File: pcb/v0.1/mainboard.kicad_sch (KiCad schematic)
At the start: 9 parts, among them J11 USB_C_Receptacle_fw, J12 Conn_01x02_Pin, J6 Conn_01x04_Pin, U6 AP2112K-3.3TRG1

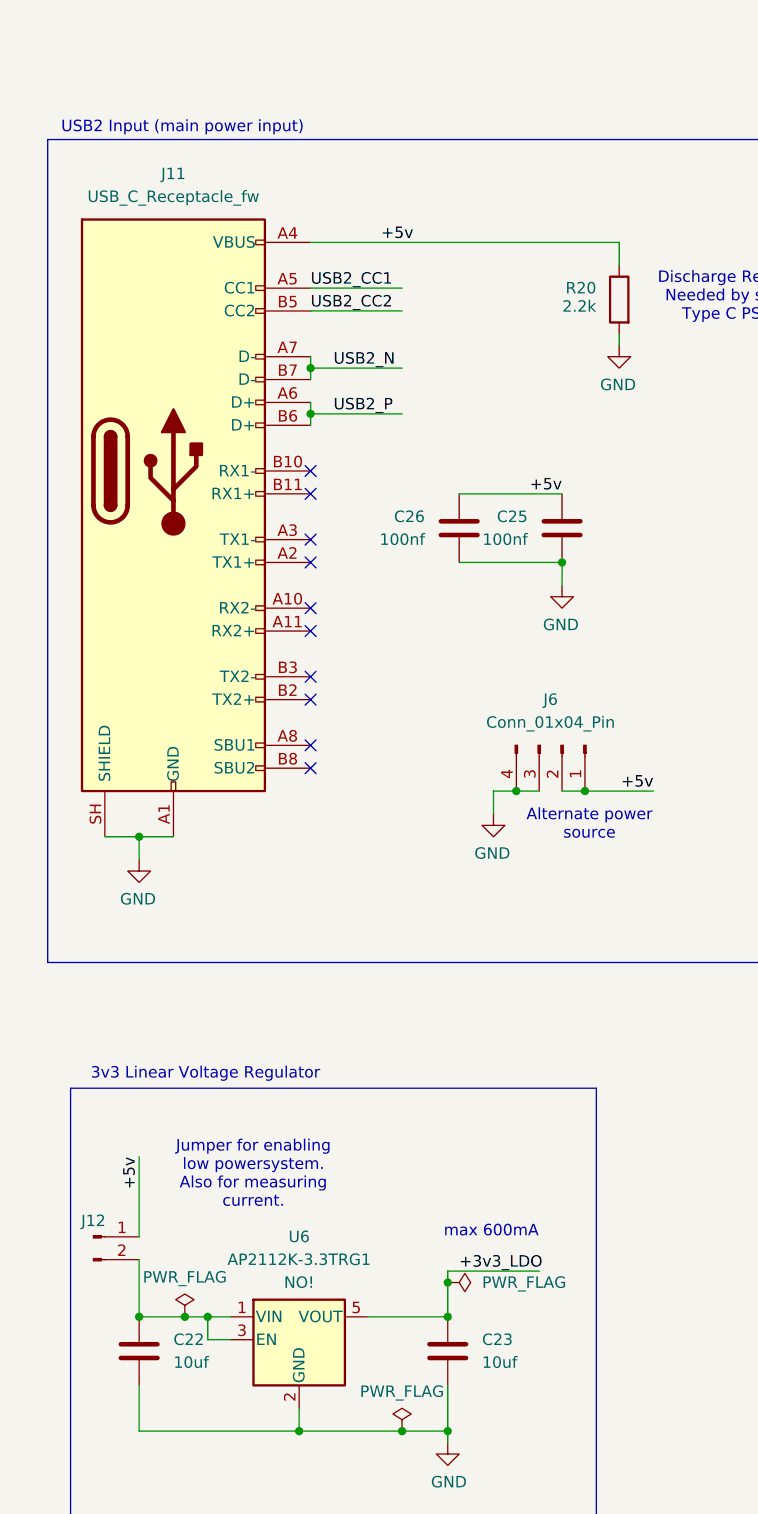
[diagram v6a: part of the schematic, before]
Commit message: Add pullup for nRESET of the nRF.
Also re-annotated all of the symbol numbers as they were starting to get
out of hand.
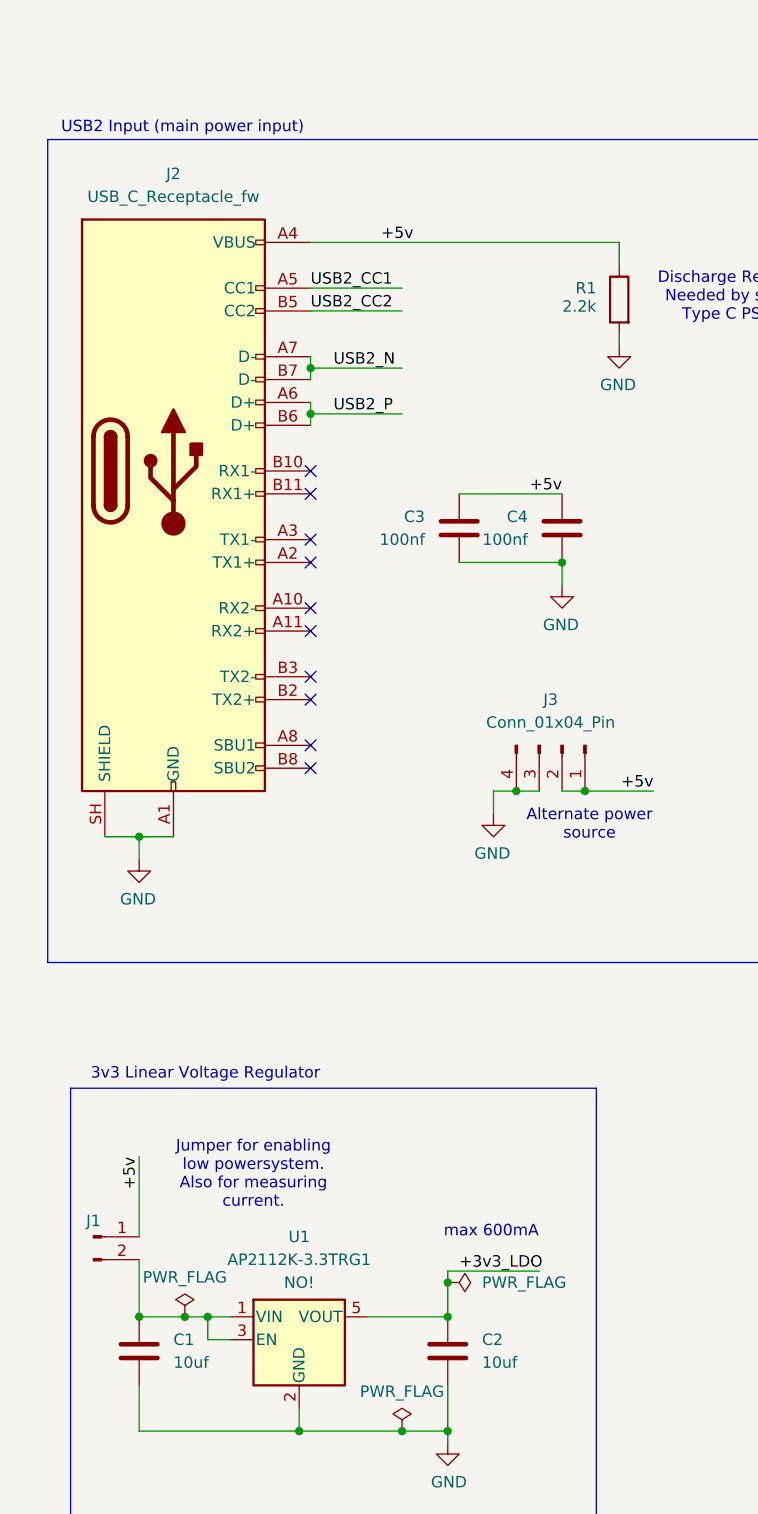
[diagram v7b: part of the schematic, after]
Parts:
- renumbered C22 to C1, C23 to C2, C26 to C3, C25 to C4, J12 to J1, J11 to J2, J6 to J3, R20 to R1, U6 to U1
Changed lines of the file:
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@@
 		(dnp no)
 		(fields_autoplaced yes)
-		(property "Reference" "C26"
+		(property "Reference" "C3"
 			(at 62.23 71.12 0)
 			(show_name no)
@@
 			(project "mainboard"
 				(path "/5b8aa782-5c3d-43e7-a869-3bd000015f52"
-					(reference "C26")
+					(reference "C3")
 					(unit 1)
 				)
@@
 		(dnp no)
 		(fields_autoplaced yes)
-		(property "Reference" "C22"
+		(property "Reference" "C1"
 			(at 34.29 162.5599 0)
 			(show_name no)
@@
 			(project "mainboard"
 				(path "/5b8aa782-5c3d-43e7-a869-3bd000015f52"
-					(reference "C22")
+					(reference "C1")
 					(unit 1)
 				)
@@
 		(in_pos_files yes)
 		(dnp no)
-		(property "Reference" "J12"
+		(property "Reference" "J1"
 			(at 25.4 149.352 0)
 			(show_name no)
@@
 			(project "mainboard"
 				(path "/5b8aa782-5c3d-43e7-a869-3bd000015f52"
-					(reference "J12")
+					(reference "J1")
 					(unit 1)
 				)
@@
 		(in_pos_files yes)
 		(dnp no)
-		(property "Reference" "#PWR040"
+		(property "Reference" "#PWR02"
 			(at 64.77 180.34 0)
 			(hide yes)
@@
 			(project "mainboard"
 				(path "/5b8aa782-5c3d-43e7-a869-3bd000015f52"
-					(reference "#PWR040")
+					(reference "#PWR02")
 					(unit 1)
 				)
@@
 		(in_pos_files yes)
 		(dnp no)
-		(property "Reference" "#PWR047"
+		(property "Reference" "#PWR01"
 			(at 30.48 115.57 0)
 			(hide yes)
@@
 			(project "mainboard"
 				(path "/5b8aa782-5c3d-43e7-a869-3bd000015f52"
-					(reference "#PWR047")
+					(reference "#PWR01")
 					(unit 1)
 				)
@@
 		(in_pos_files yes)
 		(dnp no)
-		(property "Reference" "R20"
+		(property "Reference" "R1"
 			(at 81.28 45.72 0)
 			(show_name no)
@@
 			(project "mainboard"
 				(path "/5b8aa782-5c3d-43e7-a869-3bd000015f52"
-					(reference "R20")
+					(reference "R1")
 					(unit 1)
 				)
@@
 		(in_pos_files yes)
 		(dnp no)
-		(property "Reference" "#PWR048"
+		(property "Reference" "#PWR03"
 			(at 69.85 110.49 0)
 			(hide yes)
@@
 			(project "mainboard"
 				(path "/5b8aa782-5c3d-43e7-a869-3bd000015f52"
-					(reference "#PWR048")
+					(reference "#PWR03")
 					(unit 1)
 				)
@@
 		(dnp no)
 		(fields_autoplaced yes)
-		(property "Reference" "C23"
+		(property "Reference" "C2"
 			(at 68.58 162.5599 0)
 			(show_name no)
@@
 			(project "mainboard"
 				(path "/5b8aa782-5c3d-43e7-a869-3bd000015f52"
-					(reference "C23")
+					(reference "C2")
 					(unit 1)
 				)
@@
 		(dnp no)
 		(fields_autoplaced yes)
-		(property "Reference" "U6"
+		(property "Reference" "U1"
 			(at 48.26 151.13 0)
 			(show_name no)
@@
 			(project "mainboard"
 				(path "/5b8aa782-5c3d-43e7-a869-3bd000015f52"
-					(reference "U6")
+					(reference "U1")
 					(unit 1)
 				)
@@
 		(dnp no)
 		(fields_autoplaced yes)
-		(property "Reference" "J6"
+		(property "Reference" "J3"
 			(at 76.2 91.44 90)
 			(show_name no)
@@
 			(project "mainboard"
 				(path "/5b8aa782-5c3d-43e7-a869-3bd000015f52"
-					(reference "J6")
+					(reference "J3")
 					(unit 1)
 				)
@@
 		(dnp no)
 		(fields_autoplaced yes)
-		(property "Reference" "C25"
+		(property "Reference" "C4"
 			(at 73.66 71.12 0)
 			(show_name no)
@@
 			(project "mainboard"
 				(path "/5b8aa782-5c3d-43e7-a869-3bd000015f52"
-					(reference "C25")
+					(reference "C4")
 					(unit 1)
 				)
@@
 		(in_pos_files yes)
 		(dnp no)
-		(property "Reference" "#PWR039"
+		(property "Reference" "#PWR04"
 			(at 77.47 85.09 0)
 			(hide yes)
@@
 			(project "mainboard"
 				(path "/5b8aa782-5c3d-43e7-a869-3bd000015f52"
-					(reference "#PWR039")
+					(reference "#PWR04")
 					(unit 1)
 				)
@@
 		(in_pos_files yes)
 		(dnp no)
-		(property "Reference" "J11"
+		(property "Reference" "J2"
 			(at 34.29 33.02 0)
 			(show_name no)
@@
 			(project "mainboard"
 				(path "/5b8aa782-5c3d-43e7-a869-3bd000015f52"
-					(reference "J11")
+					(reference "J2")
 					(unit 1)
 				)
@@
 		(in_pos_files yes)
 		(dnp no)
-		(property "Reference" "#PWR046"
+		(property "Reference" "#PWR05"
 			(at 83.82 58.42 0)
 			(hide yes)
@@
 			(project "mainboard"
 				(path "/5b8aa782-5c3d-43e7-a869-3bd000015f52"
-					(reference "#PWR046")
+					(reference "#PWR05")
 					(unit 1)
 				)

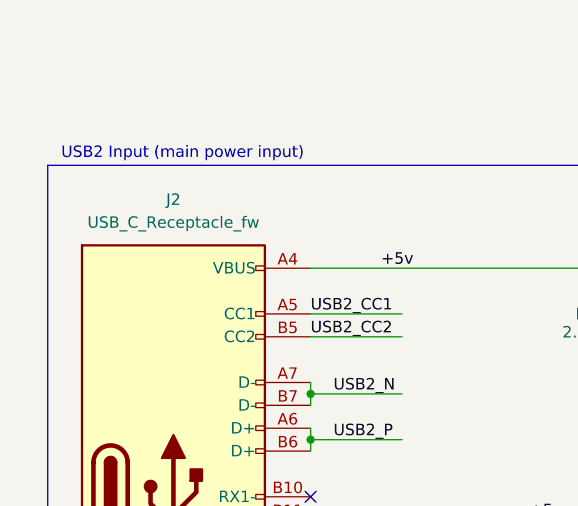
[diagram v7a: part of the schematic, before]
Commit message: Base setup for FW usb ports
The USB system is not complete yet, but all of the basics are done. The
current limit switch, its capacitors, and usb connector parts are
sorted.

However, the current limit, CC pins and second port are not configured
yet.
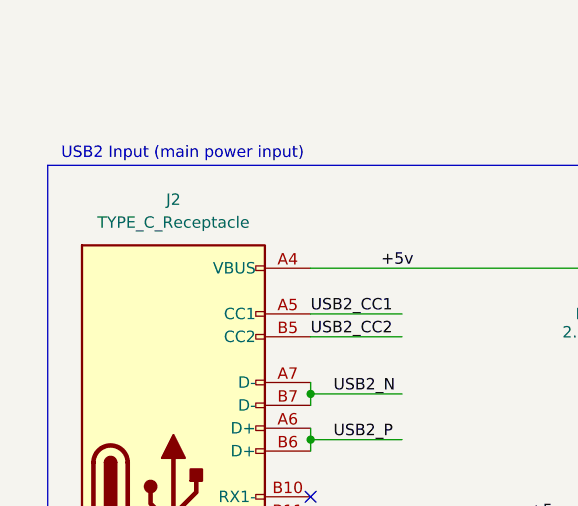
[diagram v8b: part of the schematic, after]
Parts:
- removed J2: USB_C_Receptacle_fw, symbol TH-1-CC:USB_C_Receptacle_fw
- added J2: TYPE_C_Receptacle, symbol TH-1-CC:TYPE_C_Receptacle
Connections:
- net +5v: now also J2.A4 (VBUS), J2.A9 (VBUS), J2.B4 (VBUS), J2.B9 (VBUS)
- net GND: now also J2.A1 (GND), J2.A12 (GND), J2.B1 (GND), J2.B12 (GND), J2.SH (SHIELD)
- net USB2_CC1: now also J2.A5 (CC1)
- net USB2_CC2: now also J2.B5 (CC2)
- net USB2_N: now also J2.A7 (D-), J2.B7 (D-)
- net USB2_P: now also J2.A6 (D+), J2.B6 (D+)
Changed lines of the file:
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@@
+	)
+	(symbol
+		(lib_id "TH-1-CC:TYPE_C_Receptacle")
+		(at 34.29 66.04 0)
+		(unit 1)
+		(body_style 1)
+		(exclude_from_sim no)
+		(in_bom yes)
+		(on_board yes)
+		(in_pos_files yes)
+		(dnp no)
+		(fields_autoplaced yes)
+		(property "Reference" "J2"
+			(at 34.29 33.02 0)
+			(show_name no)
+			(do_not_autoplace no)
+			(effects
+				(font
+					(size 1.27 1.27)
+				)
+			)
+		)
+		(property "Value" "TYPE_C_Receptacle"
+			(at 34.29 35.56 0)
+			(show_name no)
+			(do_not_autoplace no)
+			(effects
+				(font
+					(size 1.27 1.27)
+				)
+			)
+		)
+		(property "Footprint" ""
+			(at 38.1 66.04 0)
+			(hide yes)
+			(show_name no)
+			(do_not_autoplace no)
+			(effects
+				(font
+					(size 1.27 1.27)
+				)
+			)
+		)
+		(property "Datasheet" "https://www.molex.com/pdm_docs/ps/PS-105448-001.pdf"
+			(at 38.1 66.04 0)
+			(hide yes)
+			(show_name no)
+			(do_not_autoplace no)
+			(effects
+				(font
+					(size 1.27 1.27)
+				)
+			)
+		)
+		(property "Description" "USB Full-Featured Type-C Receptacle connector"
+			(at 34.29 66.04 0)
+			(hide yes)
+			(show_name no)
+			(do_not_autoplace no)
+			(effects
+				(font
+					(size 1.27 1.27)
+				)
+			)
+		)
+		(property "Manufacturer" "MOLEX"
+			(at 34.29 66.04 0)
+			(hide yes)
+			(show_name no)
+			(do_not_autoplace no)
+			(effects
+				(font
+					(size 1.27 1.27)
+				)
+			)
+		)
+		(property "Mfr. Part no" "1054500101"
+			(at 34.29 66.04 0)
+			(hide yes)
+			(show_name no)
+			(do_not_autoplace no)
+			(effects
+				(font
+					(size 1.27 1.27)
+				)
+			)
+		)
+		(property "Distributor Digikey" "https://www.digikey.co.uk/en/products/detail/molex/1054500101/5843890"
+			(at 34.29 66.04 0)
+			(hide yes)
+			(show_name no)
+			(do_not_autoplace no)
+			(effects
+				(font
+					(size 1.27 1.27)
+				)
+			)
+		)
+		(property "Digikey Part no" "WM12856TR-ND"
+			(at 34.29 66.04 0)
+			(hide yes)
+			(show_name no)
+			(do_not_autoplace no)
+			(effects
+				(font
+					(size 1.27 1.27)
+				)
+			)
+		)
+		(property "Stock" "NO!"
+			(at 34.29 66.04 0)
+			(hide yes)
+			(show_name no)
+			(do_not_autoplace no)
+			(effects
+				(font
+					(size 1.27 1.27)
+				)
+			)
+		)
+		(pin "B5"
+		)
+		(pin "B6"
+		)
+		(pin "B11"
+		)
+		(pin "SH"
+		)
+		(pin "B7"
+		)
+		(pin "B8"
+		)
+		(pin "B9"
+		)
+		(pin "B12"
+		)
+		(pin "B10"
+		)
+		(pin "A6"
+		)
+		(pin "A7"
+		)
+		(pin "A8"
+		)
+		(pin "A9"
+		)
+		(pin "A10"
+		)
+		(pin "A11"
+		)
+		(pin "A12"
+		)
+		(pin "B1"
+		)
+		(pin "B2"
+		)
+		(pin "B3"
+		)
+		(pin "B4"
+		)
+		(pin "A1"
+		)
+		(pin "A2"
+		)
+		(pin "A3"
+		)
+		(pin "A4"
+		)
+		(pin "A5"
+		)
+		(instances
+			(project "mainboard"
+				(path "/5b8aa782-5c3d-43e7-a869-3bd000015f52"
+					(reference "J2")
+					(unit 1)
+				)
+			)
+		)
 	)
 	(symbol
@@
 					(unit 1)
 				)
-			)
-		)
-	)
-	(symbol
-		(lib_id "TH-1-CC:USB_C_Receptacle_fw")
-		(at 34.29 66.04 0)
-		(unit 1)
-		(body_style 1)
-		(exclude_from_sim no)
-		(in_bom yes)
-		(on_board yes)
-		(in_pos_files yes)
-		(dnp no)
-		(property "Reference" "J2"
-			(at 34.29 33.02 0)
-			(show_name no)
-			(do_not_autoplace no)
-			(effects
-				(font
-					(size 1.27 1.27)
-				)
-			)
-		)
-		(property "Value" "USB_C_Receptacle_fw"
-			(at 34.29 35.56 0)
-			(show_name no)
-			(do_not_autoplace no)
-			(effects
-				(font
-					(size 1.27 1.27)
-				)
-			)
-		)
-		(property "Footprint" ""
-			(at 38.1 66.04 0)
-			(hide yes)
-			(show_name no)
-			(do_not_autoplace no)
-			(effects
-				(font
-					(size 1.27 1.27)
-				)
-			)
-		)
-		(property "Datasheet" "https://gct.co/files/specs/usb4056-spec.pdf"
-			(at 38.1 66.04 0)
-			(hide yes)
-			(show_name no)
-			(do_not_autoplace no)
-			(effects
-				(font
-					(size 1.27 1.27)
-				)
-			)
-		)
-		(property "Description" "USB Full-Featured Type-C Receptacle connector"
-			(at 34.29 66.04 0)
-			(hide yes)
-			(show_name no)
-			(do_not_autoplace no)
-			(effects
-				(font
-					(size 1.27 1.27)
-				)
-			)
-		)
-		(property "Manufacturer" "GCT"
-			(at 34.29 66.04 0)
-			(hide yes)
-			(show_name no)
-			(do_not_autoplace no)
-			(effects
-				(font
-					(size 1.27 1.27)
-				)
-			)
-		)
-		(property "Mfr. Part no" "USB4056-03-A"
-			(at 34.29 66.04 0)
-			(hide yes)
-			(show_name no)
-			(do_not_autoplace no)
-			(effects
-				(font
-					(size 1.27 1.27)
-				)
-			)
-		)
-		(property "Distributor Digikey" "https://www.digikey.co.uk/en/products/detail/gct/USB4056-03-A/14638038"
-			(at 34.29 66.04 0)
-			(hide yes)
-			(show_name no)
-			(do_not_autoplace no)
-			(effects
-				(font
-					(size 1.27 1.27)
-				)
-			)
-		)
-		(property "Digikey Part no" "2073-USB4056-03-ATR-ND"
-			(at 34.29 66.04 0)
-			(hide yes)
-			(show_name no)
-			(do_not_autoplace no)
-			(effects
-				(font
-					(size 1.27 1.27)
-				)
-			)
-		)
-		(property "Stock" "NO!"
-			(at 34.29 66.04 0)
-			(hide yes)
-			(show_name no)
-			(do_not_autoplace no)
-			(effects
-				(font
-					(size 1.27 1.27)
-				)
-			)
-		)
-		(pin "A11"
-		)
-		(pin "B7"
-		)
-		(pin "B1"
-		)
-		(pin "B4"
-		)
-		(pin "A12"
-		)
-		(pin "B6"
-		)
-		(pin "A9"
-		)
-		(pin "B11"
-		)
-		(pin "B2"
-		)
-		(pin "B12"
-		)
-		(pin "A7"
-		)
-		(pin "A6"
-		)
-		(pin "A5"
-		)
-		(pin "A4"
-		)
-		(pin "A3"
-		)
-		(pin "A2"
-		)
-		(pin "A1"
-		)
-		(pin "B3"
-		)
-		(pin "A10"
-		)
-		(pin "B5"
-		)
-		(pin "B8"
-		)
-		(pin "SH"
-		)
-		(pin "A8"
-		)
-		(pin "B10"
-		)
-		(pin "B9"
-		)
-		(instances
-			(project "mainboard"
-				(path "/5b8aa782-5c3d-43e7-a869-3bd000015f52"
-					(reference "J2")
-					(unit 1)
-				)
